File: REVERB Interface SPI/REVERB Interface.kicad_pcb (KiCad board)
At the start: 2 copper layers, 90.2 x 95.9 mm, 58 parts, among them J1 RPiZeroW, J2 Iridium, J3 APRS, J4 Antenna, M1 MountingHole_Pad, M2 MountingHole_Pad, M3 MountingHole_Pad, M4 MountingHole_Pad, M5 PiMount, M6 PiMount, M7 PiMount, M8 PiMount, U1 LSM9DS1BOB, U2 MAX3232, U3 SC16IS752IPW, Y1 1.8432MHz

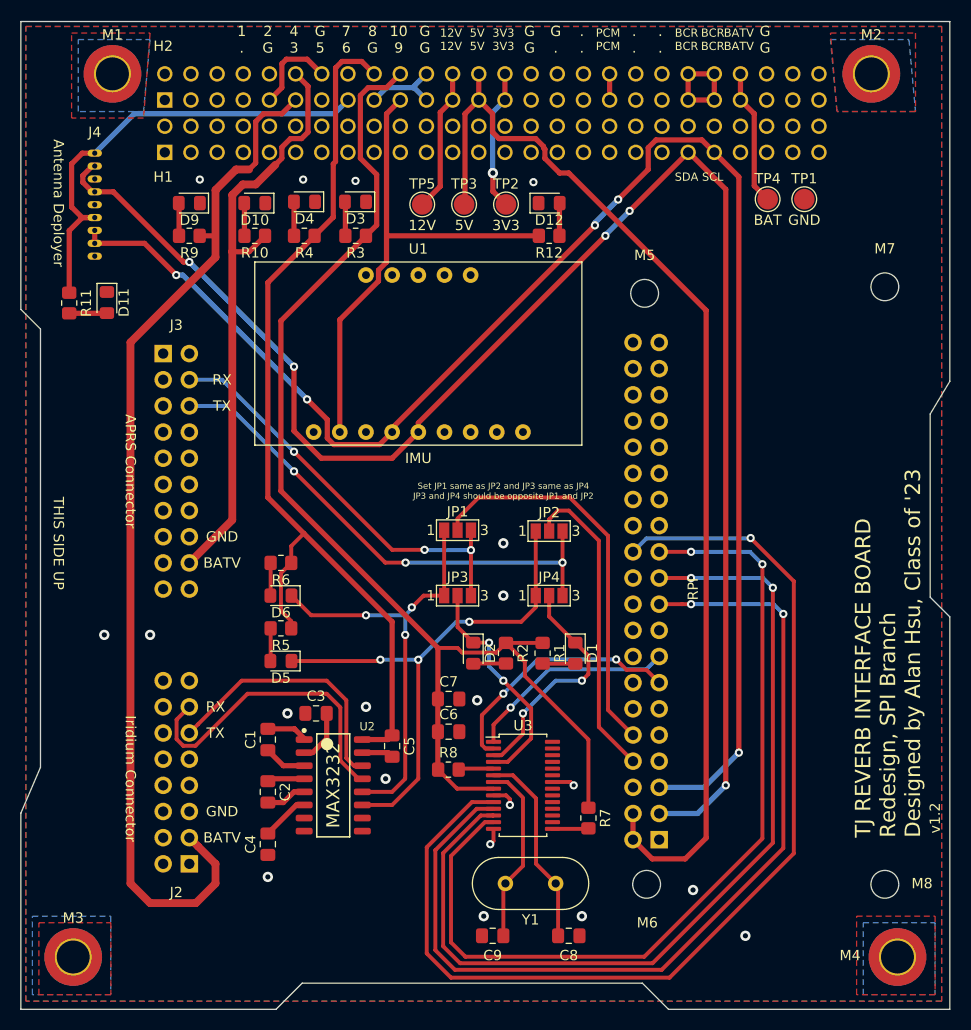
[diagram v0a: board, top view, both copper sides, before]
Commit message: Remove incorrect uart flow control connections, pull CTS low. Improve silkscreen placement
Issue #3 and Issue #5
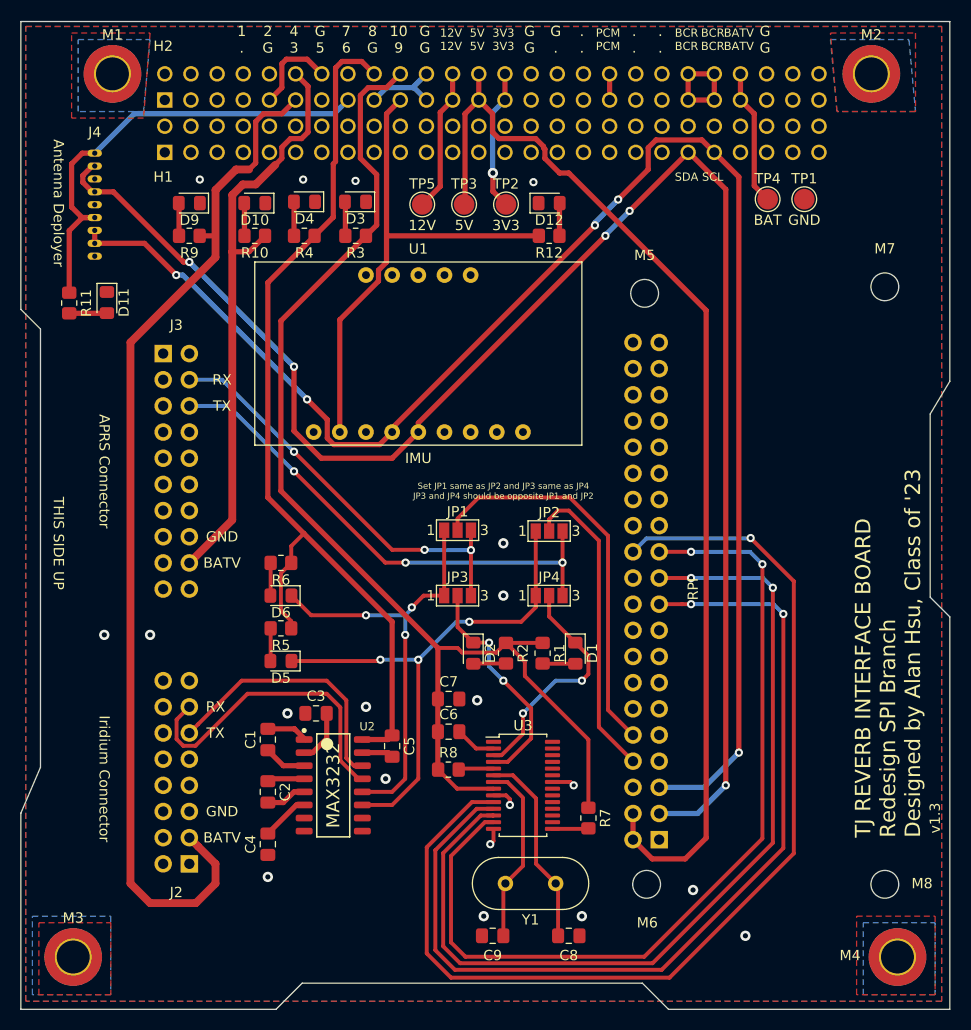
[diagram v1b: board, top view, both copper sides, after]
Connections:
- J1 pad 13: /CTS -> (no net)
- J1 pad 15: /RTS -> (no net)
- U3 pad 1: /RTS -> (no net)
- U3 pad 2: /CTS -> GND
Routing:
- net /CTS: track 24.5 -> 0.00 mm, vias 2 -> 0
- net /RTS: track 20.5 -> 0.00 mm, vias 1 -> 0
- net GND: track 25.9 -> 29.9 mm
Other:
- board text added: "TJ REVERB INTERFACE BOARD Redesign SPI Branch Designed by Alan Hsu, Class of '23"
- board text added: "v1.3"
- board text removed: "TJ REVERB INTERFACE BOARD Redesign, SPI Branch Designed by Alan Hsu, Class of '23"
- board text removed: "v1.2"

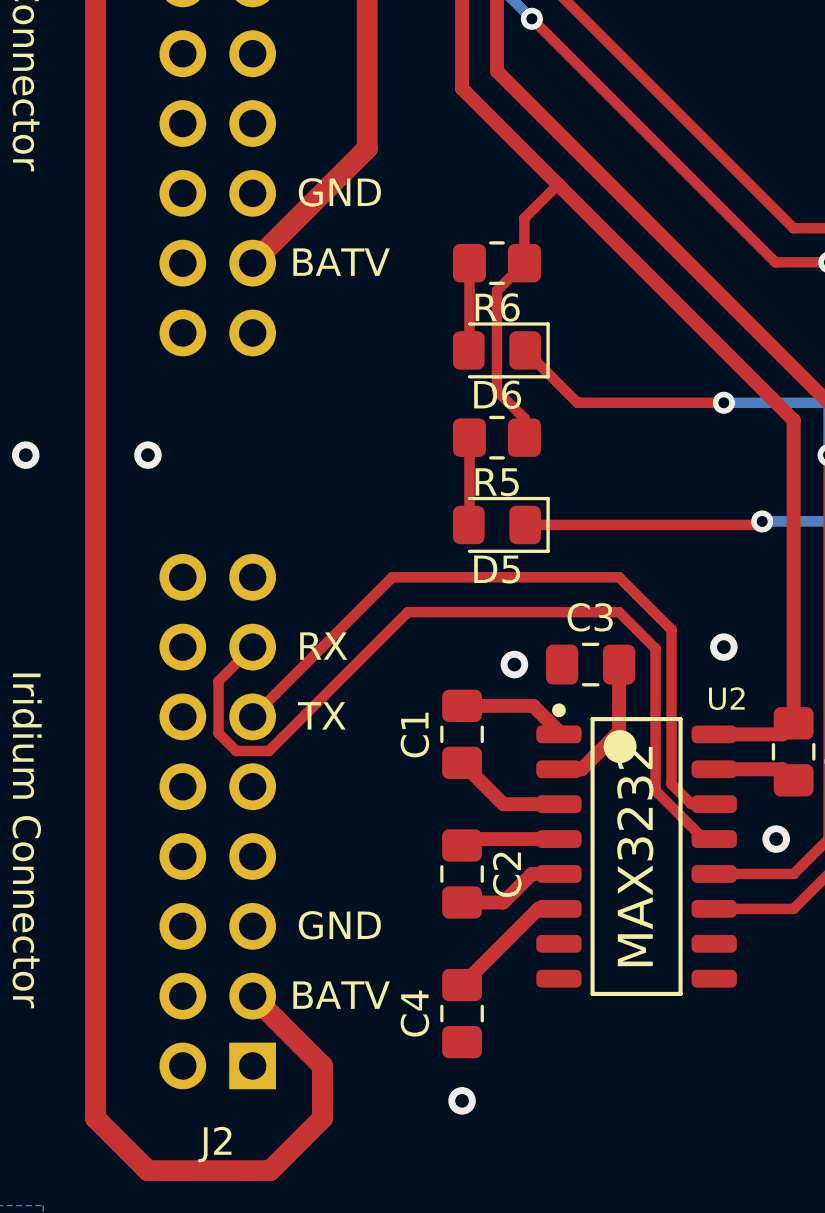
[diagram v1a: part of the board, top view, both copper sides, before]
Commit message: Improve usb branch silkscreen, push v1.3
#5 Will need to verify required clearance for connector housing later.
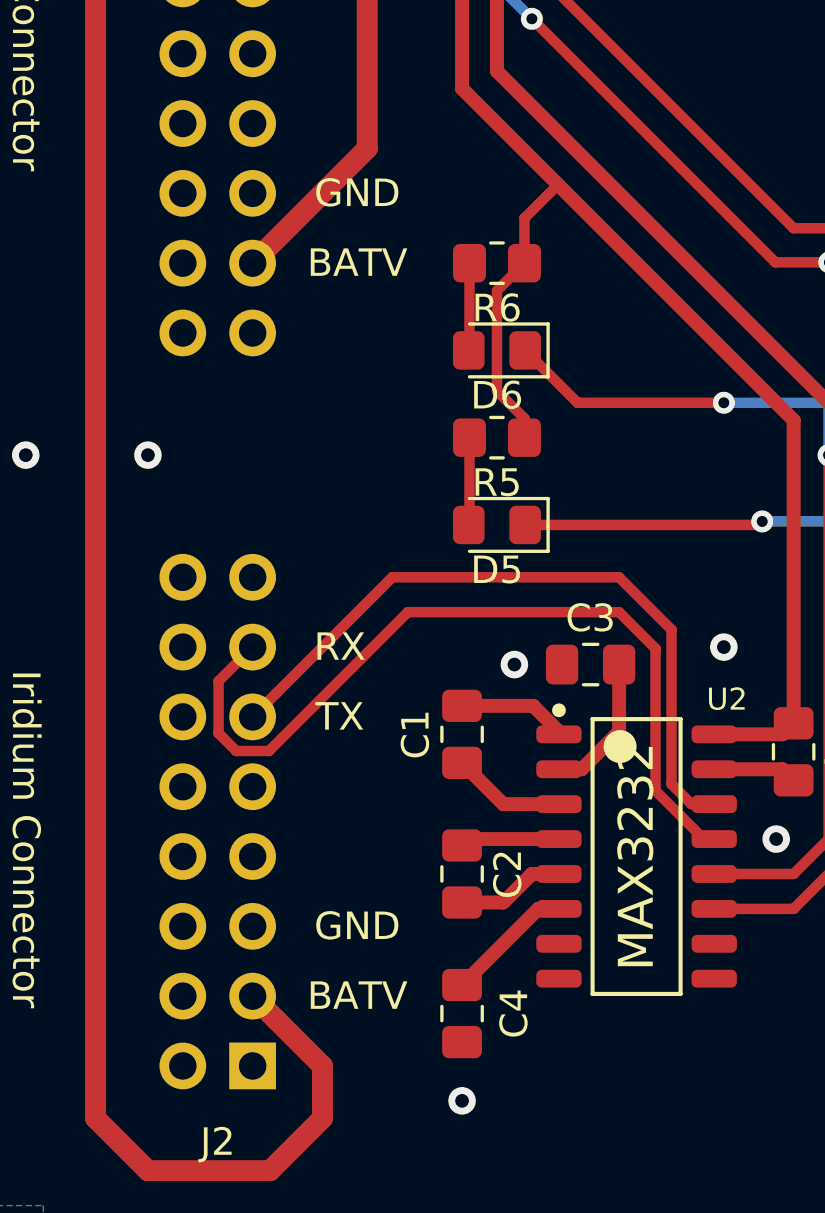
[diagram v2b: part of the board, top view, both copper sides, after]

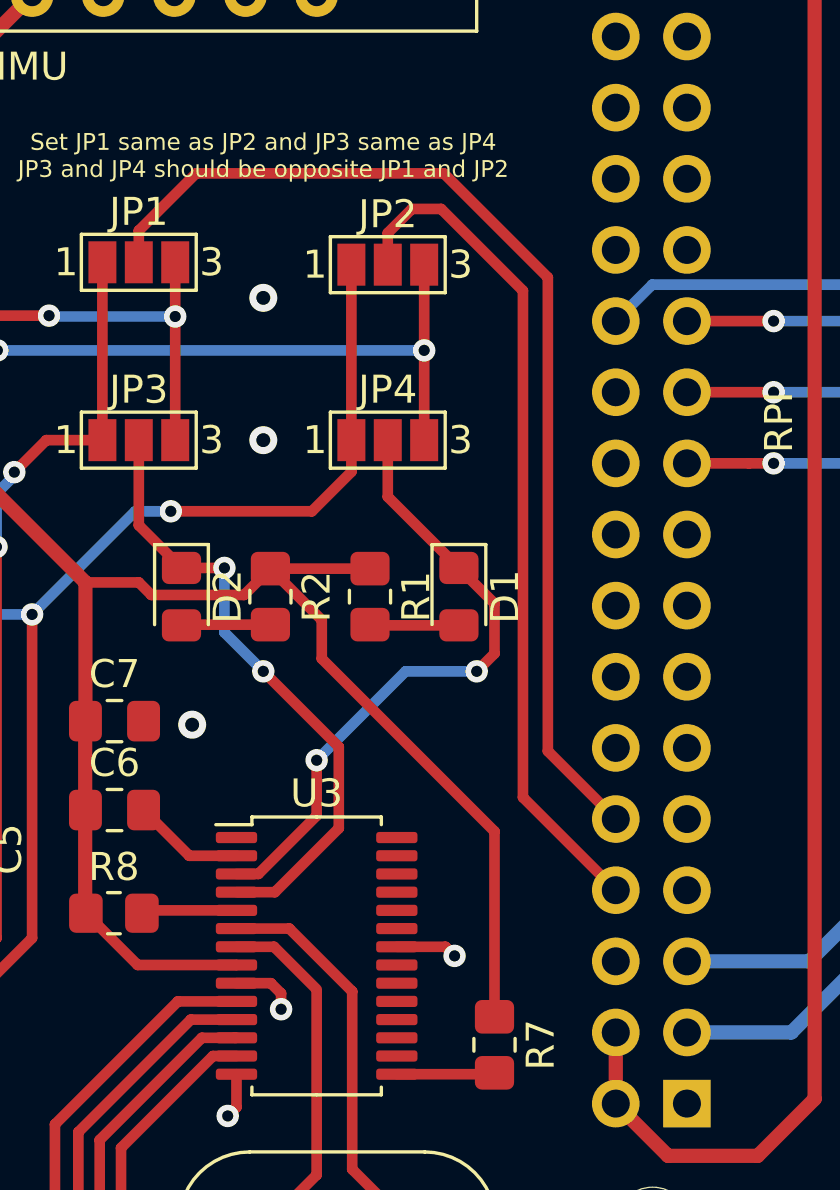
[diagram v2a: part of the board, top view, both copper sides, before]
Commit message: Add bitbang uart connections
gpio 23 and 24, #2
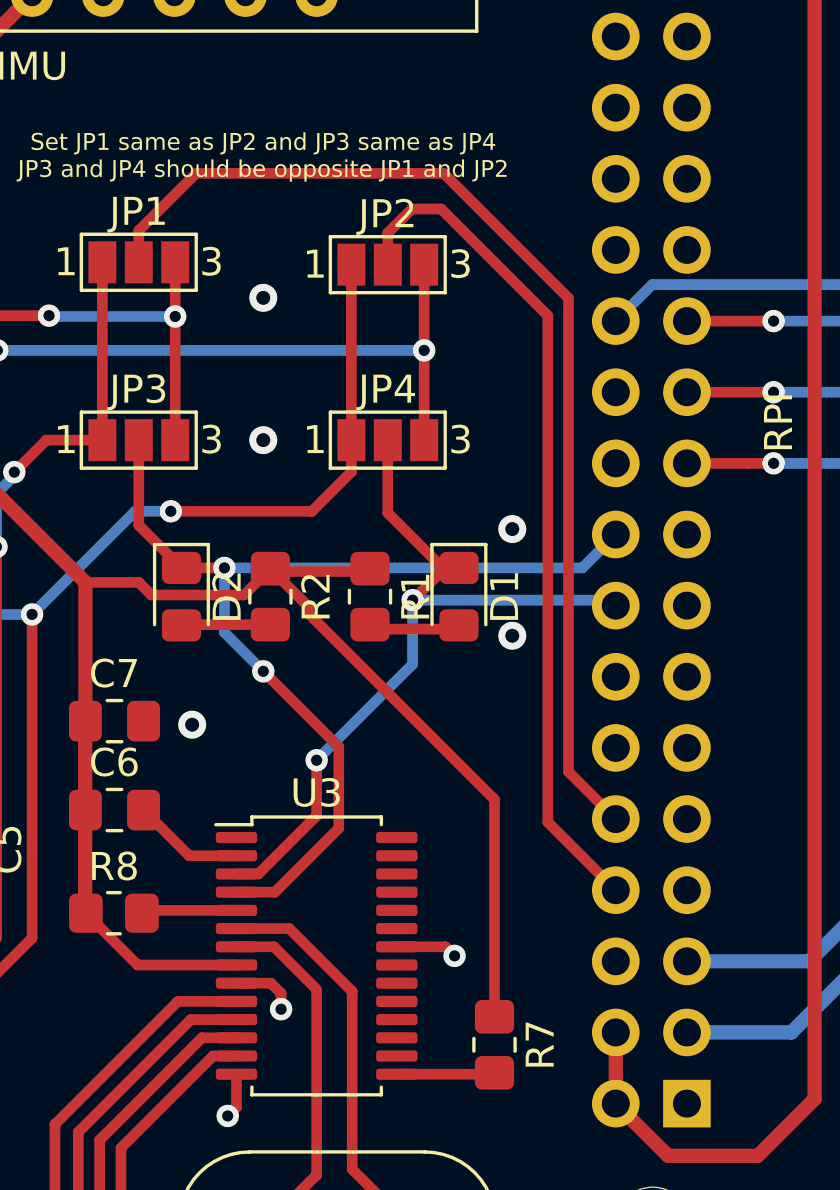
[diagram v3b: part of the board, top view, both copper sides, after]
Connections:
- J1 pad 16: (no net) -> /SPIUARTTX
- J1 pad 18: (no net) -> /SPIUARTRX
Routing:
- net /SPIUARTRX: track 22.3 -> 36.8 mm
- net /SPIUARTTX: track 22.8 -> 28.3 mm
- net GND: vias 20 -> 22

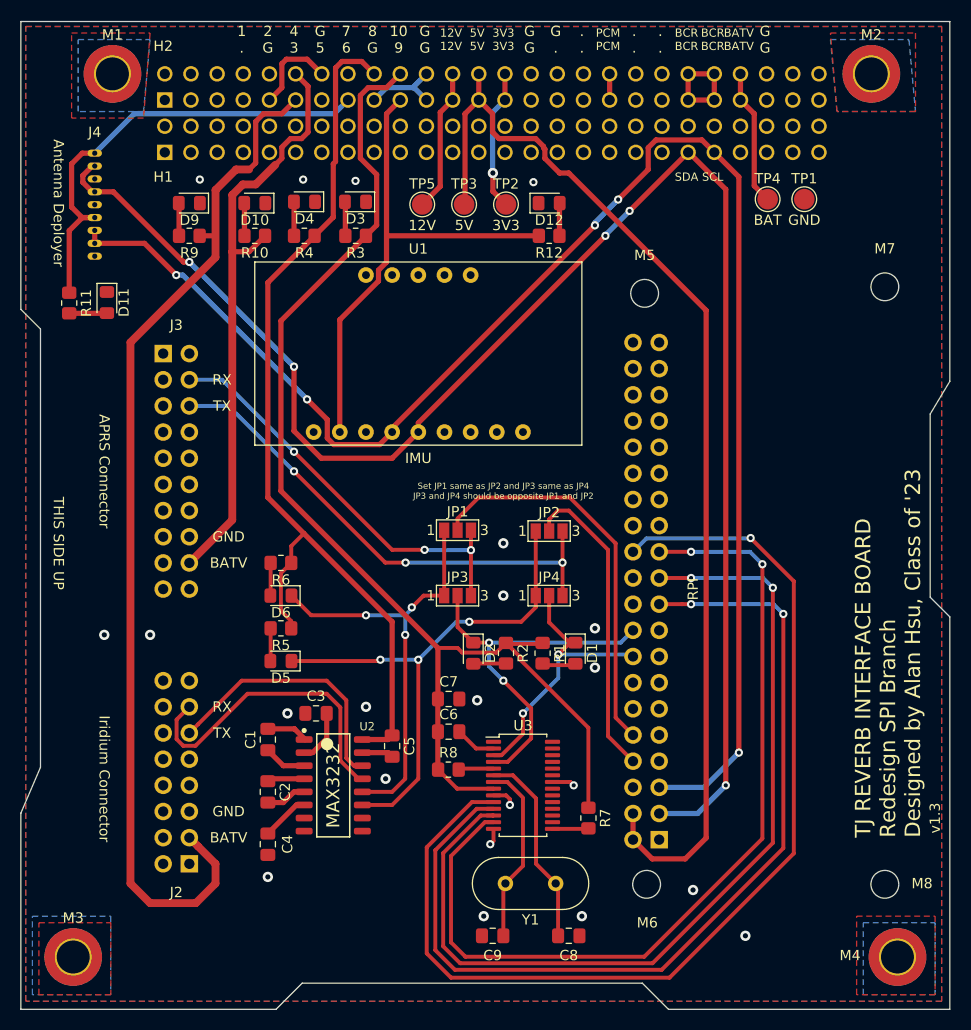
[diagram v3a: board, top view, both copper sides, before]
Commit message: add level shifter to routing
#1
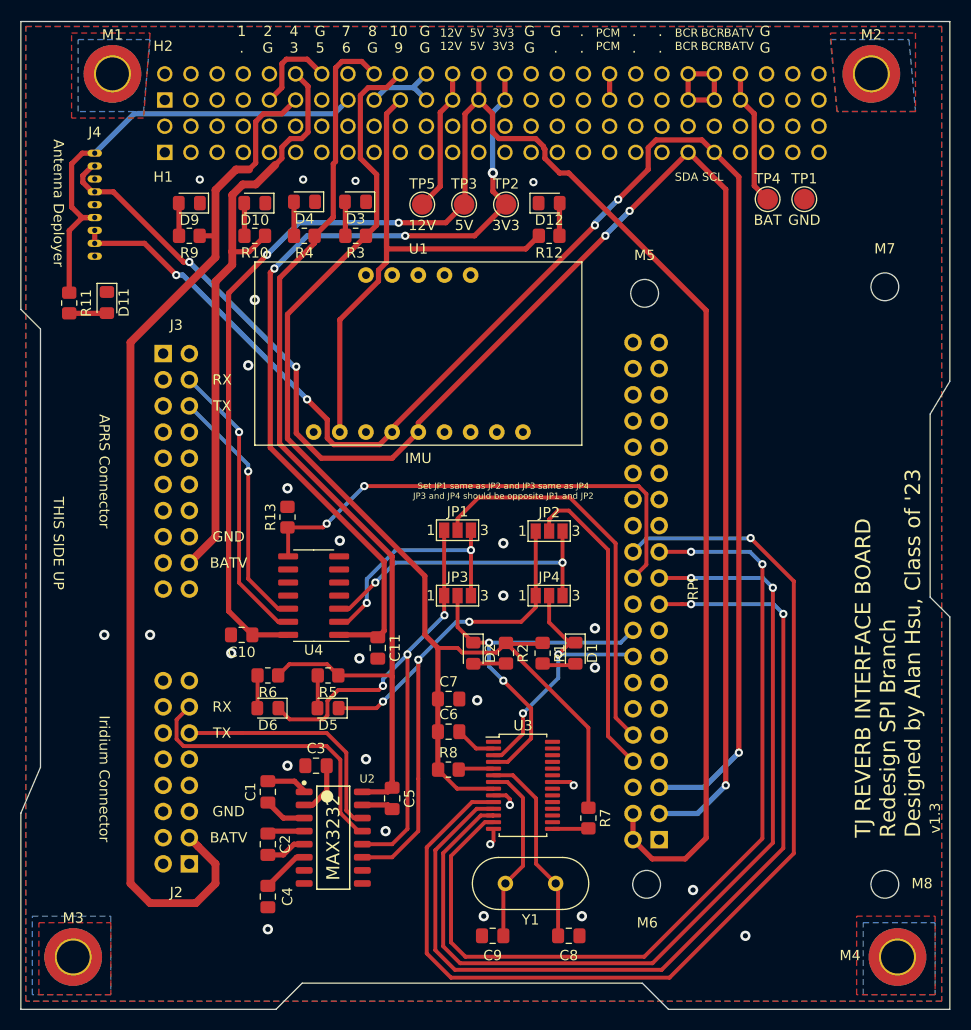
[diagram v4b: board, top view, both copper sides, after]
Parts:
- added C10: 0.1uF, Capacitor_SMD:C_0805_2012Metric_Pad1.18x1.45mm_HandSolder, F.Cu at (128.3, 112.4)
- added C11: 0.1uF, Capacitor_SMD:C_0805_2012Metric_Pad1.18x1.45mm_HandSolder, F.Cu at (141.5, 113.7)
- added R13: 10K, Resistor_SMD:R_0805_2012Metric_Pad1.20x1.40mm_HandSolder, F.Cu at (132.7, 101.0)
- added U4: TXB0104D, Package_SO:SOIC-14_3.9x8.7mm_P1.27mm, F.Cu at (135.3, 108.6)
- moved D6 11.0 mm to (130.8, 119.5)
- moved R6 11.0 mm to (130.8, 116.3)
- moved D5 6.47 mm to (136.7, 119.5)
- moved R5 6.47 mm to (136.7, 116.3)
- moved C5 5.08 mm to (142.9, 128.3)
- moved U2 5.08 mm to (137.2, 132.1)
- moved C1 5.08 mm to (130.8, 127.6)
- moved C2 5.08 mm to (130.8, 132.7)
- moved C3 5.08 mm to (135.5, 125.1)
- moved C4 5.08 mm to (130.8, 137.8)
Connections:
- J1 pad 22: (no net) -> /OE
- J3 pad 4: /APRSRX -> /APRSRXSh
- J3 pad 6: /APRSTX -> /APRSTXSh
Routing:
- net +3V3: track 13.7 -> 83.4 mm, vias 1 -> 3
- net +5V: track 107.9 -> 171.9 mm, vias 0 -> 2
- net /OE: track 0.00 -> 48.3 mm, vias 0 -> 2
- net /APRSRXSh: track 0.00 -> 28.0 mm, vias 0 -> 1
- net /APRSTXSh: track 0.00 -> 24.2 mm, vias 0 -> 1
- net /APRSTX: track 48.8 -> 29.8 mm, vias 3 -> 2
- net /APRSRX: track 40.5 -> 23.4 mm, vias 3 -> 2
- net /R1OUT: track 43.5 -> 52.4 mm
- net /SW8: track 90.7 -> 96.3 mm
- net /T1IN: track 51.4 -> 54.2 mm
- net /T1OUT: track 25.5 -> 23.4 mm
- net /R1IN: track 30.4 -> 28.3 mm
- net /SW9: track 49.5 -> 51.2 mm
- net /SW10: track 117.9 -> 117.4 mm
- net GND: vias 22 -> 28
